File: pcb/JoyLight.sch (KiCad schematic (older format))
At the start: 27 parts, among them J1 110990037, J2 110990037, J3 110990037, J4 110990037, J5 Conn_01x07_Male, J6 Conn_01x07_Male, SW1 SW_SPST, SW2 SW_SPST, SW3 SW_SPST, U1 SeeeduinoXIAO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

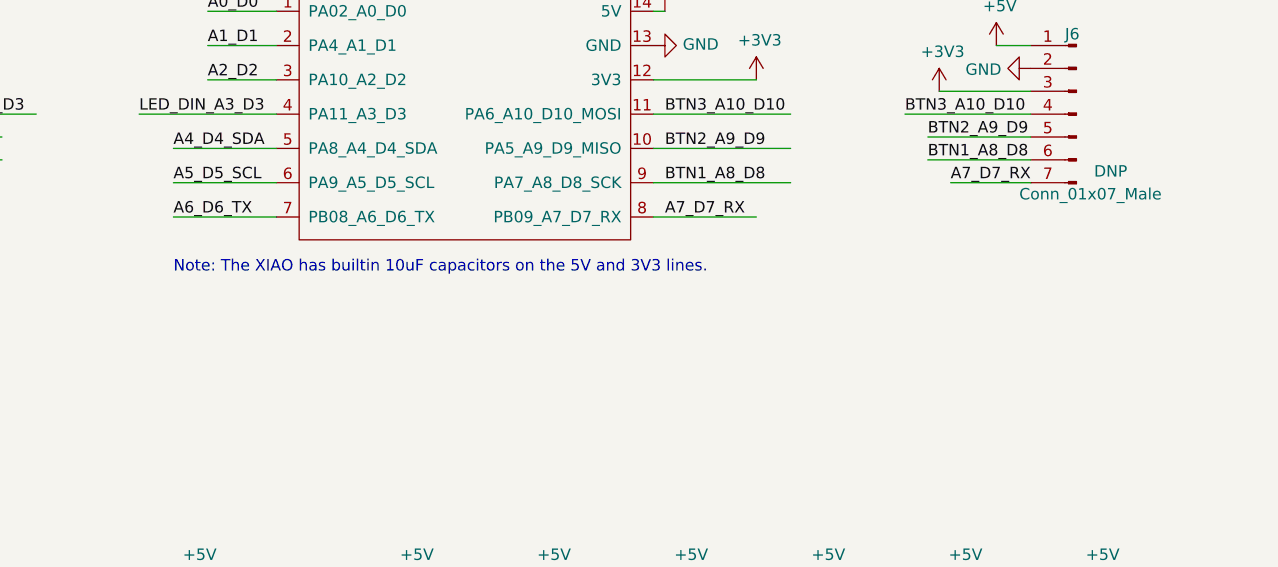
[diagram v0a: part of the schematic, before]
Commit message: Changed the mounting method of the Xiao
The Xiao is now mounted by using the pin headers supplied with it instead of directly soldering it to the board
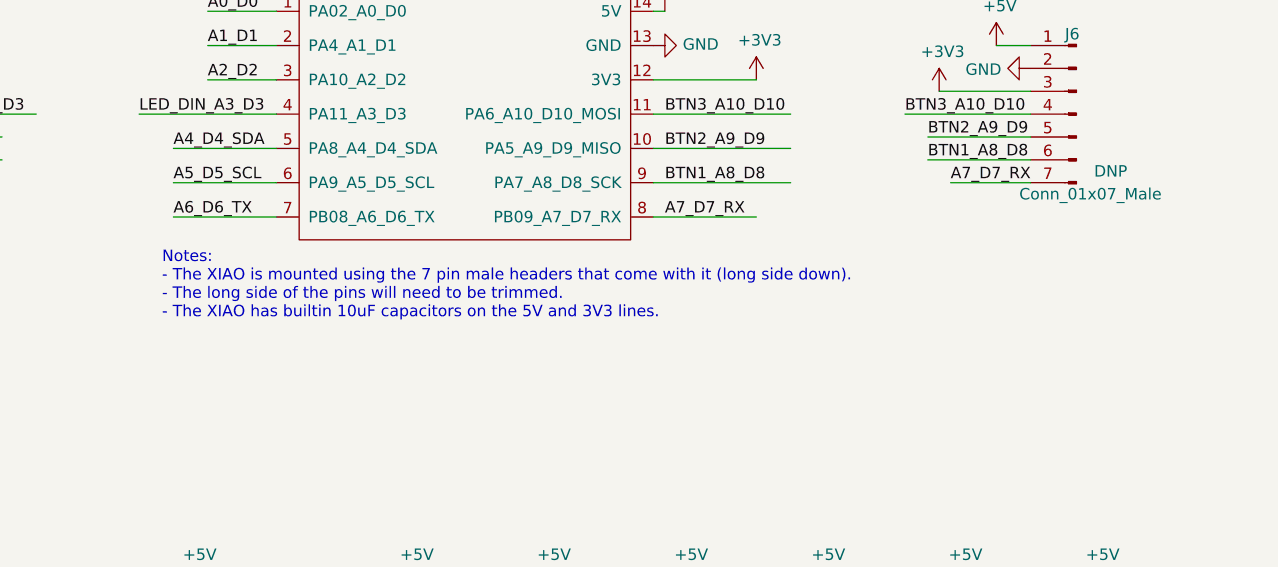
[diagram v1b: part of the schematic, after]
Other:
- note added: "Notes: \n- The XIAO is mounted using the 7 pin male headers that come with it (long side down). \n- The long side of the pins will need to be trimmed.\n- The XIAO has builtin 10uF capacitors on the 5V and 3V3 lines."
- note removed: "Note: The XIAO has builtin 10uF capacitors on the 5V and 3V3 lines."
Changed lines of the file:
@@
 Wire Wire Line
 	2950 4500 3200 4500
-Text Notes 2450 2800 0    50   ~ 0
-Note: The XIAO has builtin 10uF capacitors on the 5V and 3V3 lines.
+Text Notes 2400 3000 0    50   ~ 0
+Notes: \n- The XIAO is mounted using the 7 pin male headers that come with it (long side down). \n- The long side of the pins will need to be trimmed.\n- The XIAO has builtin 10uF capacitors on the 5V and 3V3 lines.
 $EndSCHEMATC

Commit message: PCB finishing touches
- added mounting points
- added the OSHW logo
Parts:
- added H1, H2, H3, H4: MountingHole, MountingHole:MountingHole_3.2mm_M3, symbol Mechanical:MountingHole
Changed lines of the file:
@@
 Text Notes 2400 3000 0    50   ~ 0
 Notes: \n- The XIAO is mounted using the 7 pin male headers that come with it (long side down). \n- The long side of the pins will need to be trimmed.\n- The XIAO has builtin 10uF capacitors on the 5V and 3V3 lines.
+$Comp
+L Mechanical:MountingHole H2
+U 1 1 60360E68
+P 9450 3300
+F 0 "H2" H 9550 3346 50  0000 L CNN
+F 1 "MountingHole" H 9550 3255 50  0000 L CNN
+F 2 "MountingHole:MountingHole_3.2mm_M3" H 9450 3300 50  0001 C CNN
+F 3 "~" H 9450 3300 50  0001 C CNN
+	1    9450 3300
+	1    0    0    -1
+$EndComp
+$Comp
+L Mechanical:MountingHole H4
+U 1 1 603620E1
+P 9450 3500
+F 0 "H4" H 9550 3546 50  0000 L CNN
+F 1 "MountingHole" H 9550 3455 50  0000 L CNN
+F 2 "MountingHole:MountingHole_3.2mm_M3" H 9450 3500 50  0001 C CNN
+F 3 "~" H 9450 3500 50  0001 C CNN
+	1    9450 3500
+	1    0    0    -1
+$EndComp
+$Comp
+L Mechanical:MountingHole H1
+U 1 1 6036263C
+P 8700 3300
+F 0 "H1" H 8800 3346 50  0000 L CNN
+F 1 "MountingHole" H 8800 3255 50  0000 L CNN
+F 2 "MountingHole:MountingHole_3.2mm_M3" H 8700 3300 50  0001 C CNN
+F 3 "~" H 8700 3300 50  0001 C CNN
+	1    8700 3300
+	1    0    0    -1
+$EndComp
+$Comp
+L Mechanical:MountingHole H3
+U 1 1 603628A8
+P 8700 3500
+F 0 "H3" H 8800 3546 50  0000 L CNN
+F 1 "MountingHole" H 8800 3455 50  0000 L CNN
+F 2 "MountingHole:MountingHole_3.2mm_M3" H 8700 3500 50  0001 C CNN
+F 3 "~" H 8700 3500 50  0001 C CNN
+	1    8700 3500
+	1    0    0    -1
+$EndComp
 $EndSCHEMATC

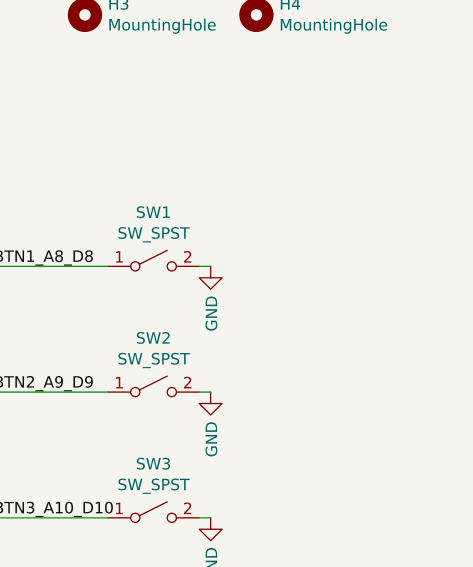
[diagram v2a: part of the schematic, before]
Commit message: Updated schematic
Missed these files in the previous commit
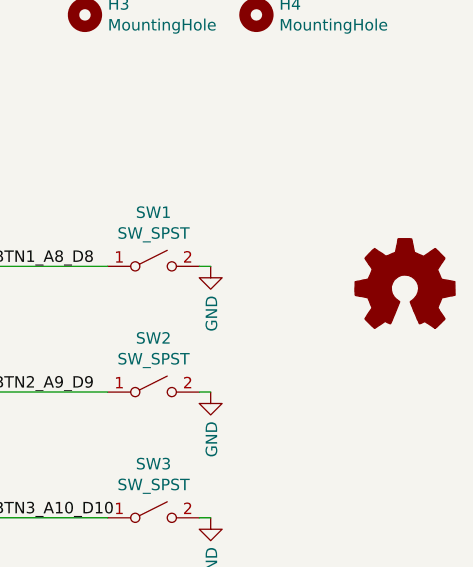
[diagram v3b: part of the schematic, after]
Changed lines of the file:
@@
+	1    0    0    -1
+$EndComp
+$Comp
+L Graphic:Logo_Open_Hardware_Small #LOGO1
+U 1 1 60382BF3
+P 10100 4700
+F 0 "#LOGO1" H 10100 4975 50  0001 C CNN
+F 1 "Logo_Open_Hardware_Small" H 10100 4475 50  0001 C CNN
+F 2 "" H 10100 4700 50  0001 C CNN
+F 3 "~" H 10100 4700 50  0001 C CNN
+	1    10100 4700
 	1    0    0    -1
 $EndComp
